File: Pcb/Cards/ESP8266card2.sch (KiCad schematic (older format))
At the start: 15 parts, among them P1 Debug-SoftSerial-FTDI, P2 ESP-Programming-FTDI, P3 CA6_CONN_01X10, U1 ESP-12E/F, U2 74??08tbd

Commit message: Partial changes to ESP8266card2 before merge with updated CA6 main board for 2x6 header, etc.
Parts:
- removed P1: Debug-SoftSerial-FTDI, Pin_Headers:Pin_Header_Angled_1x06_Pitch2.54mm, symbol FTDI
- removed R9: 1K, CA6:SM0603_Resistor, symbol R
- removed U2: 74??08tbd, symbol 74LS08
- added J?: CONN_01X02, symbol CONN_01X02
- added U?: SN74AHC1G08, SOT-23-5, symbol SN74AHC1G08
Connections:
- wire segments 68 -> 76
- no-connect marks 14 -> 11
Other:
- note removed: "Elim. if low AND current??"
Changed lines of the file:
@@
 LIBS:contrib
 LIBS:valves
+LIBS:ESP8266card2-cache
 EELAYER 25 0
 EELAYER END
@@
 	7300 2900 7650 2900
 Wire Wire Line
-	3550 3550 3550 3850
+	3550 3550 3550 3650
+Wire Wire Line
+	3550 3650 3550 3850
 Connection ~ 3550 3650
 $Comp
@@
 $EndComp
 Wire Wire Line
-	7750 4250 7750 4550
+	7750 4250 7750 4400
+Wire Wire Line
+	7750 4400 7750 4550
 $Comp
 L R R8
@@
 $EndComp
 Wire Wire Line
-	8100 3950 8100 4150
+	8100 3950 8100 4050
+Wire Wire Line
+	8100 4050 8100 4150
 Connection ~ 8100 4050
 $Comp
@@
 $EndComp
 Wire Wire Line
-	3850 4350 4550 4350
+	3850 4350 4100 4350
+Wire Wire Line
+	4100 4350 4400 4350
+Wire Wire Line
+	4400 4350 4550 4350
 Connection ~ 4400 4350
 Wire Wire Line
-	4100 4750 4400 4750
+	4100 4750 4250 4750
+Wire Wire Line
+	4250 4750 4400 4750
 $Comp
 L GND #PWR4
@@
 Connection ~ 7750 4400
 $Comp
-L FTDI P1
-U 1 1 58BF42D5
-P 1950 4200
-F 0 "P1" H 1950 3800 50  0000 C CNN
-F 1 "Debug-SoftSerial-FTDI" H 1950 4600 50  0000 C CNN
-F 2 "Pin_Headers:Pin_Header_Angled_1x06_Pitch2.54mm" H 1950 4200 50  0001 C CNN
-F 3 "DOCUMENTATION" H 1950 4200 50  0001 C CNN
-	1    1950 4200
-	-1   0    0    1
-$EndComp
-$Comp
 L GND #PWR1
 U 1 1 58BF45F7
-P 2750 4450
-F 0 "#PWR1" H 2750 4200 50  0001 C CNN
-F 1 "GND" H 2750 4300 50  0000 C CNN
-F 2 "" H 2750 4450 50  0000 C CNN
-F 3 "" H 2750 4450 50  0000 C CNN
-	1    2750 4450
-	1    0    0    -1
-$EndComp
-Text Label 6800 4950 1    60   ~ 0
+P 7050 5100
+F 0 "#PWR1" H 7050 4850 50  0001 C CNN
+F 1 "GND" H 7050 4950 50  0000 C CNN
+F 2 "" H 7050 5100 50  0000 C CNN
+F 3 "" H 7050 5100 50  0000 C CNN
+	1    7050 5100
+	1    0    0    -1
+$EndComp
+Text Label 6800 4850 1    60   ~ 0
 Debug-TX
 Text Label 4100 4250 0    60   ~ 0
@@
 	5200 1700 5200 3200
 Wire Wire Line
-	6350 2800 6350 3650
+	6350 2800 6350 3150
+Wire Wire Line
+	6350 3150 6350 3650
 Text Label 6350 3550 1    60   ~ 0
 ESP_TX
-NoConn ~ 2600 3950
-NoConn ~ 2600 4250
-NoConn ~ 2600 4350
 Wire Wire Line
 	5000 1700 4950 1700
@@
 $EndComp
 Wire Wire Line
-	6350 4150 7550 4150
+	6350 4150 6800 4150
+Wire Wire Line
+	6800 4150 7550 4150
 Wire Wire Line
 	7000 3150 6350 3150
@@
 	6050 2150 6050 2300
 Wire Wire Line
-	6350 4250 7250 4250
+	6350 4250 6900 4250
+Wire Wire Line
+	6900 4250 7250 4250
 Wire Wire Line
 	3650 3650 3550 3650
@@
 	4550 3850 4150 3850
 Wire Wire Line
-	4150 3650 4550 3650
-Wire Wire Line
-	6350 3750 7050 3750
+	4150 3650 4500 3650
+Wire Wire Line
+	4500 3650 4550 3650
+Wire Wire Line
+	6350 3750 8250 3750
 Wire Wire Line
 	7500 4050 8100 4050
 Wire Wire Line
-	6350 4050 7000 4050
+	6350 4050 6800 4050
+Wire Wire Line
+	6800 4050 7000 4050
 Wire Wire Line
 	5900 1700 5900 2150
@@
 	1    0    0    -1
 $EndComp
-$Comp
-L R R9
-U 1 1 58C41CF1
-P 7300 3750
-F 0 "R9" V 7380 3750 50  0000 C CNN
-F 1 "1K" V 7300 3750 50  0000 C CNN
-F 2 "CA6:SM0603_Resistor" V 7230 3750 50  0001 C CNN
-F 3 "" H 7300 3750 50  0000 C CNN
-	1    7300 3750
-	0    -1   -1   0
-$EndComp
 Text Label 6400 3750 0    60   ~ 0
 ESP_RX
@@
 ESP_RESET
 Wire Wire Line
-	2750 4450 2600 4450
-Wire Wire Line
-	6800 4150 6800 5200
-Wire Wire Line
-	6800 5200 2900 5200
-Wire Wire Line
-	2900 5200 2900 4050
-Wire Wire Line
-	2900 4050 2600 4050
+	6800 4150 6800 4900
 Connection ~ 6800 4150
-$Comp
-L 74LS08 U2
-U 1 1 58CC0DC9
-P 8850 3750
-F 0 "U2" H 8850 3800 50  0000 C CNN
-F 1 "74??08tbd" H 8850 3700 50  0000 C CNN
-F 2 "" H 8850 3750 50  0001 C CNN
-F 3 "" H 8850 3750 50  0001 C CNN
-	1    8850 3750
-	-1   0    0    1
-$EndComp
-Wire Wire Line
-	8250 3750 7550 3750
-Text Notes 7350 3700 0    60   ~ 0
-Elim. if low AND current??
 Text Notes 6100 2550 0    60   ~ 0
 Elim or lower??
@@
 Text Notes 1700 2250 0    60   ~ 0
 Consider lowering all 10k Pull-ups to 4.7k or ???
+$Comp
+L SN74AHC1G08 U?
+U 1 1 58D899B8
+P 8850 3750
+F 0 "U?" H 8850 3800 50  0000 C CNN
+F 1 "SN74AHC1G08" H 8850 3700 50  0000 C CNN
+F 2 "SOT-23-5" H 8800 3500 50  0001 C CNN
+F 3 "http://www.ti.com/lit/gpn/sn74ahc1g08" H 8850 4150 50  0001 C CNN
+	1    8850 3750
+	-1   0    0    1
+$EndComp
+$Comp
+L CONN_01X02 J?
+U 1 1 58D8ABB0
+P 7250 4950
+F 0 "J?" H 7250 5100 50  0000 C CNN
+F 1 "CONN_01X02" V 7350 4950 50  0000 C CNN
+F 2 "" H 7250 4950 50  0001 C CNN
+F 3 "" H 7250 4950 50  0001 C CNN
+	1    7250 4950
+	1    0    0    -1
+$EndComp
+Wire Wire Line
+	6800 4900 7050 4900
+Wire Wire Line
+	7050 5100 7050 5000
 $EndSCHEMATC

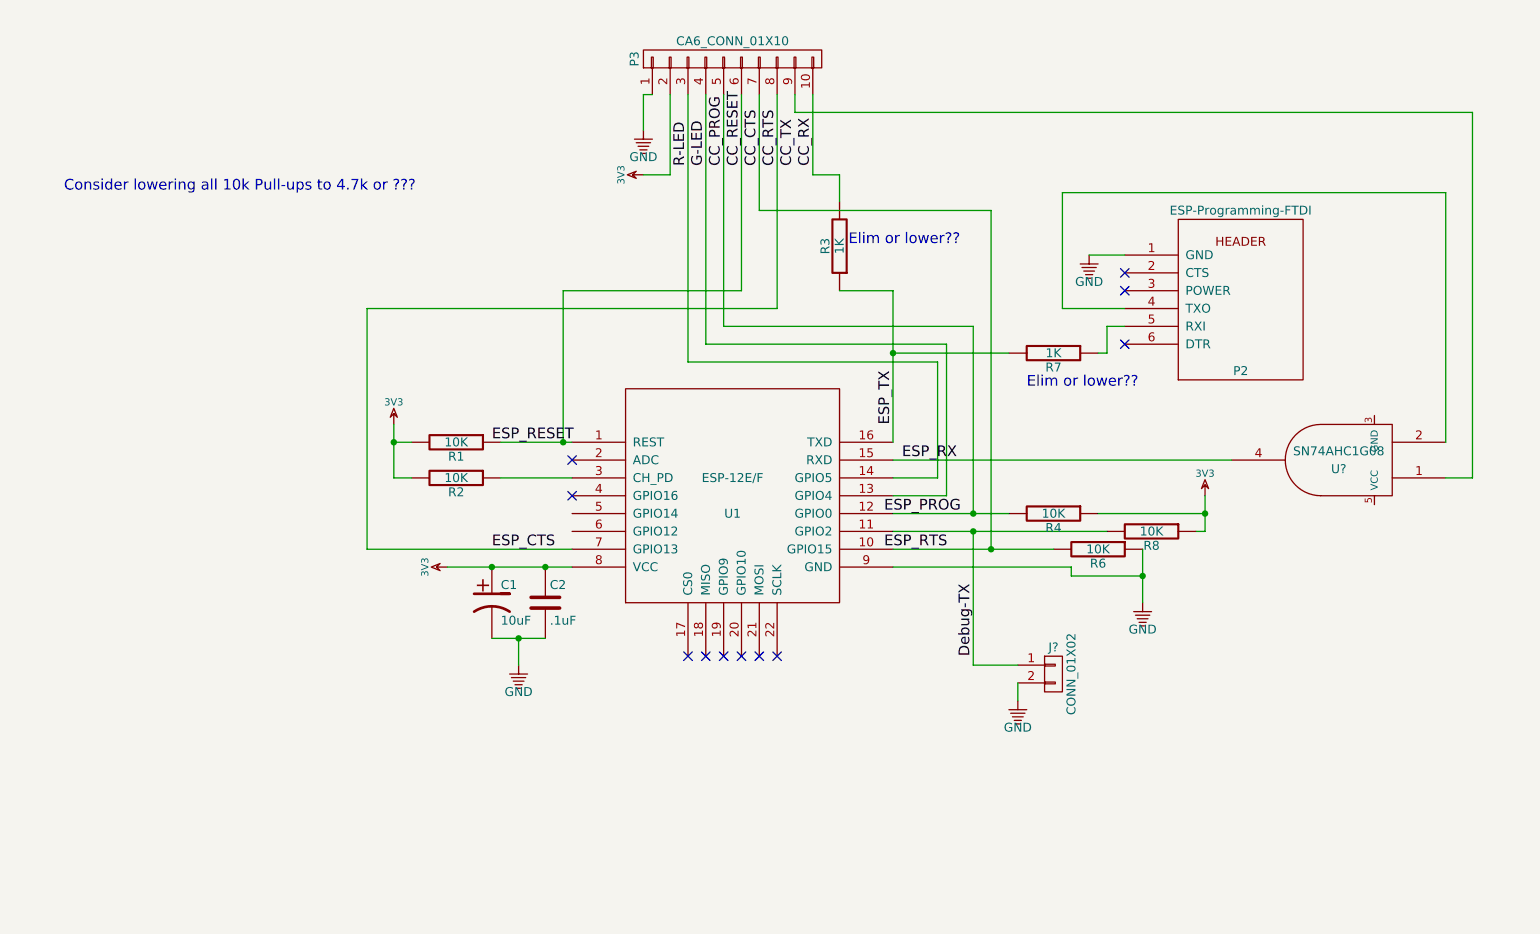
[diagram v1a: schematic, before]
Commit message: Temp commit to check and update dimensions between CA6 board and connection card
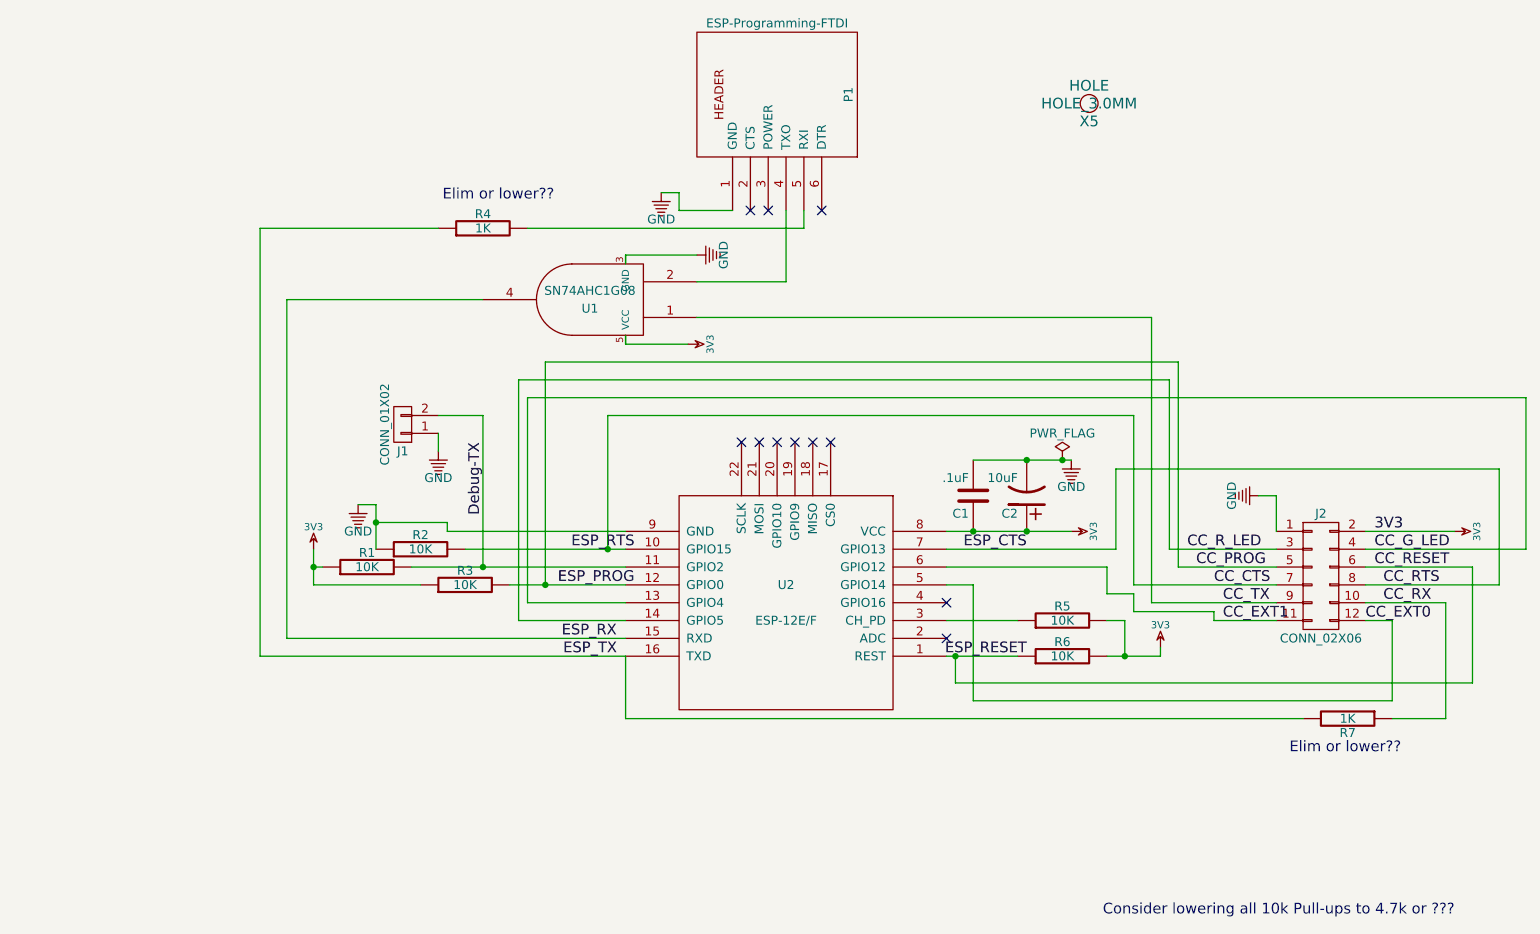
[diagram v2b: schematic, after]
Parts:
- removed P3: CA6_CONN_01X10, Pin_Header_Straight_1x10_Pitch2.54mm, symbol CONN_01X10
- added J2: CONN_02X06, Pin_Headers:Pin_Header_Straight_2x06_Pitch2.54mm, symbol CONN_02X06
- added X5: HOLE, HOLE_3.0MM, symbol HOLE
- J1: renamed from J?; footprint (none) -> Pin_Headers:Pin_Header_Angled_1x02_Pitch2.54mm
- U1: renamed from U?; footprint SOT-23-5 -> TO_SOT_Packages_SMD:SOT-23-5
- renumbered C2 to C1, C1 to C2, P2 to P1, R8 to R1, R6 to R2, R4 to R3, R7 to R4, R2 to R5, R1 to R6, R3 to R7, U1 to U2
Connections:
- net 3V3: now also U1.5 (VCC), J2.2 (P2)
- net CC_CTS: now also J2.7 (P7)
- net CC_PROG: now also J2.5 (P5)
- net CC_RESET: now also J2.6 (P6)
- net CC_RTS: now also J2.8 (P8)
- net CC_RX: now also R7.1, J2.10 (P10); no longer R7.2
- net CC_TX: now also U1.1, J2.9 (P9)
- net Debug-TX: now also J1.2 (P2); no longer J1.1 (P1)
- net ESP_TX: now also R4.1, R7.2; no longer R4.2, R7.1
- net GND: now also J1.1 (P1), U1.3 (GND), J2.1 (P1); no longer J1.2 (P2)
- net at P1.5 (RXI): now also R4.2; no longer R4.1
- net CC_EXT0: now reaches U2.5 (GPIO14)
- net CC_EXT0: now also J2.12 (P12)
- net CC_EXT1: now reaches U2.6 (GPIO12)
- net CC_EXT1: now also J2.11 (P11)
- net G-LED renamed CC_G_LED
- net CC_G_LED: now also J2.4 (P4)
- net R-LED renamed CC_R_LED
- net CC_R_LED: now also J2.3 (P3)
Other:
- moved on the sheet: C1, C2, J1, P1, R1, R2, R3, R4, R5, R6, R7, U1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

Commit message: Almost complete ESP8266card2.  Schematic updated with logic gate, removed 1k resistors, updated 2 pull-ups to 4.7k; Board has 2x6 pin connector to CA6 and stability screw.  Board routed, needs some cleanup of labels, etc.  Anyone testing ESP8266 should probably change to this schematic.
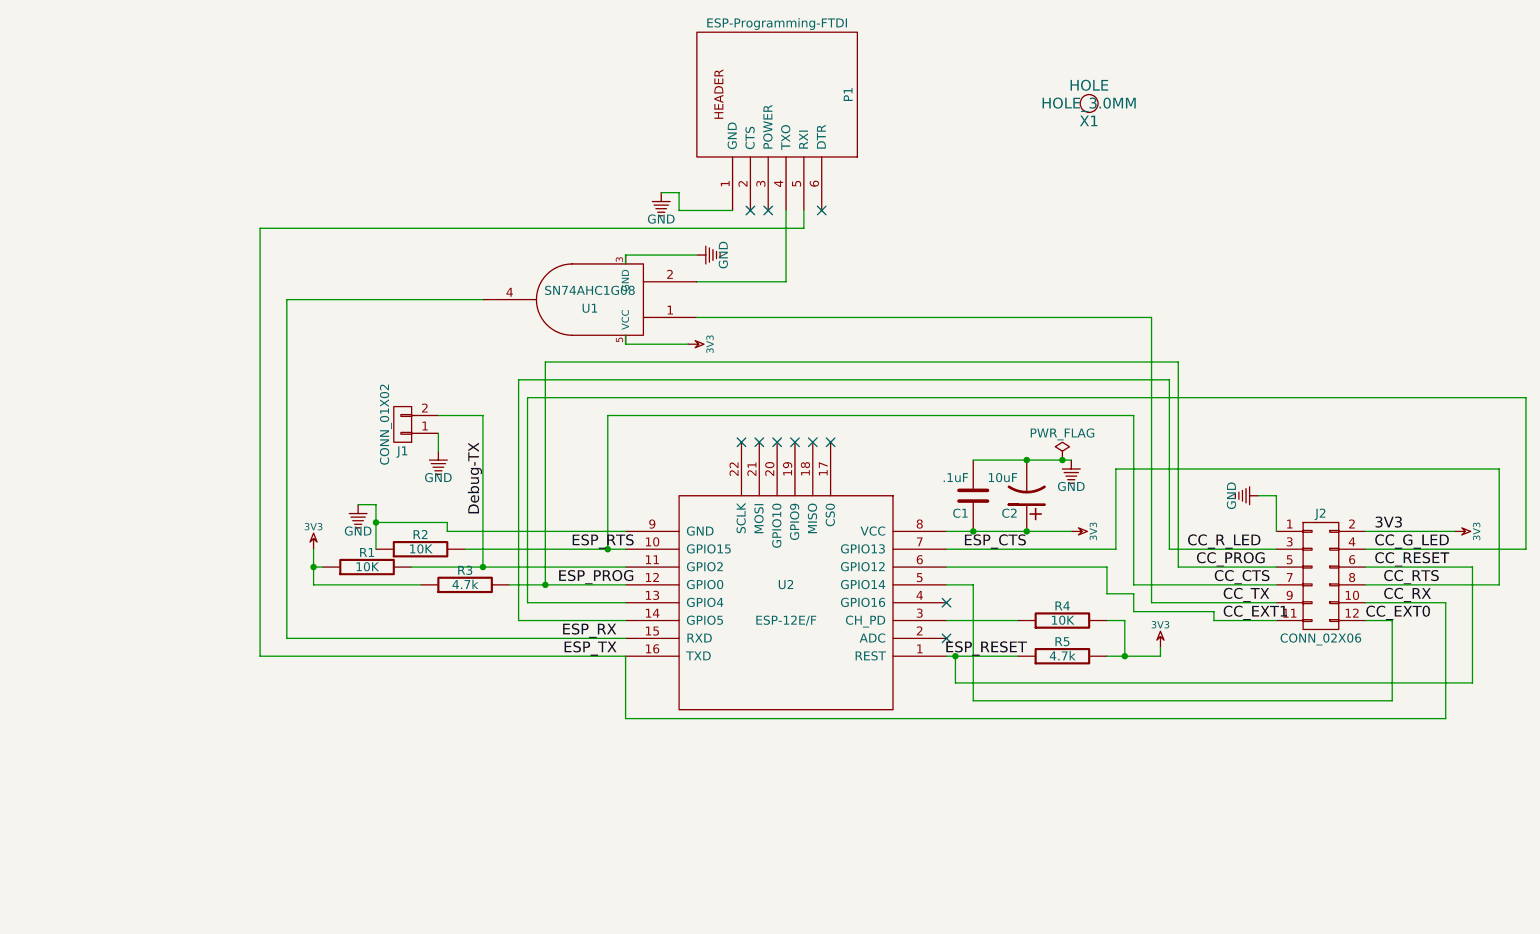
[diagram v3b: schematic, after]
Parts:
- removed R4, R7: 1K, CA6:SM0603_Resistor, symbol R
- R3: value 10K -> 4.7k
- R5: renamed from R6; value 10K -> 4.7k
- renumbered R5 to R4, X5 to X1
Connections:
- net ESP_TX is gone; now on net CC_RX: U2.16 (TXD)
- net CC_RX: now also P1.5 (RXI)
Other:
- note removed: "Consider lowering all 10k Pull-ups to 4.7k or ???"
- note removed: "Elim or lower??"
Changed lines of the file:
@@
 $EndDescr
 $Comp
-L R R6
+L R R5
 U 1 1 58C105F8
 P 7300 4850
-F 0 "R6" V 7380 4850 50  0000 C CNN
-F 1 "10K" V 7300 4850 50  0000 C CNN
+F 0 "R5" V 7380 4850 50  0000 C CNN
+F 1 "4.7k" V 7300 4850 50  0000 C CNN
 F 2 "CA6:SM0603_Resistor" V 7230 4850 50  0001 C CNN
 F 3 "" H 7300 4850 50  0000 C CNN
@@
 $EndComp
 $Comp
-L R R5
+L R R4
 U 1 1 58C106E5
 P 7300 4650
-F 0 "R5" V 7380 4650 50  0000 C CNN
+F 0 "R4" V 7380 4650 50  0000 C CNN
 F 1 "10K" V 7300 4650 50  0000 C CNN
 F 2 "CA6:SM0603_Resistor" V 7230 4650 50  0001 C CNN
@@
 P 3950 4450
 F 0 "R3" V 4030 4450 50  0000 C CNN
-F 1 "10K" V 3950 4450 50  0000 C CNN
+F 1 "4.7k" V 3950 4450 50  0000 C CNN
 F 2 "CA6:SM0603_Resistor" V 3880 4450 50  0001 C CNN
 F 3 "" H 3950 4450 50  0000 C CNN
@@
 	7650 4650 7650 4850
 Connection ~ 7650 4850
-$Comp
-L R R4
-U 1 1 58C13E97
-P 4050 2450
-F 0 "R4" V 4130 2450 50  0000 C CNN
-F 1 "1K" V 4050 2450 50  0000 C CNN
-F 2 "CA6:SM0603_Resistor" V 3980 2450 50  0001 C CNN
-F 3 "" H 4050 2450 50  0000 C CNN
-	1    4050 2450
-	0    -1   -1   0
-$EndComp
-$Comp
-L R R7
-U 1 1 58C13F04
-P 8900 5200
-F 0 "R7" V 8980 5200 50  0000 C CNN
-F 1 "1K" V 8900 5200 50  0000 C CNN
-F 2 "CA6:SM0603_Resistor" V 8830 5200 50  0001 C CNN
-F 3 "" H 8900 5200 50  0000 C CNN
-	1    8900 5200
-	0    1    1    0
-$EndComp
 $Comp
 L GND #PWR02
@@
 Wire Wire Line
 	4050 3500 4050 4350
-Text Notes 9200 5400 2    60   ~ 0
-Elim or lower??
-Text Notes 4450 2300 2    60   ~ 0
-Elim or lower??
-Text Notes 9500 6310 2    60   ~ 0
-Consider lowering all 10k Pull-ups to 4.7k or ???
 $Comp
 L SN74AHC1G08 U1
@@
 	4850 4850 4850 5200
 Wire Wire Line
-	4850 5200 8650 5200
-Wire Wire Line
-	9150 5200 9450 5200
+	4850 5200 9450 5200
 Wire Wire Line
 	9450 5200 9450 4550
@@
 	5150 2250 5050 2250
 Wire Wire Line
-	4300 2450 5850 2450
+	2800 2450 5850 2450
 Wire Wire Line
 	4850 4850 2800 4850
 Wire Wire Line
 	2800 4850 2800 2450
-Wire Wire Line
-	2800 2450 3800 2450
 Wire Wire Line
 	9000 4250 9900 4250
@@
 	7950 4350 7950 3200
 $Comp
-L HOLE X5
+L HOLE X1
 U 1 1 58DA497E
 P 7450 1750
-F 0 "X5" H 7450 1650 60  0000 C CNN
+F 0 "X1" H 7450 1650 60  0000 C CNN
 F 1 "HOLE" H 7450 1850 60  0000 C CNN
 F 2 "HOLE_3.0MM" H 7450 1750 60  0000 C CNN
